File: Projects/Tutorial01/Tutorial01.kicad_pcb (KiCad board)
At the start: 2 copper layers, 42.5 x 32.5 mm, 3 parts

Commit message: commit all
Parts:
- added REF**: MountingHole_3.2mm_M3, MountingHole:MountingHole_3.2mm_M3, F.Cu at (143.5, 89.5)
- added REF**: MountingHole_3.2mm_M3, MountingHole:MountingHole_3.2mm_M3, F.Cu at (143.5, 113.5)
- added REF**: MountingHole_3.2mm_M3, MountingHole:MountingHole_3.2mm_M3, F.Cu at (109.5, 113.5)
- added REF**: MountingHole_3.2mm_M3, MountingHole:MountingHole_3.2mm_M3, F.Cu at (109.5, 89.5)
- moved R1 18.5 mm to (141.0, 106.0), turned to 90 degrees
- moved D1 9.27 mm to (134.0, 113.5)
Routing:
- net Net-(D1-K): track 26.2 -> 10.4 mm
- net Net-(Batterie1-+): track 17.3 -> 8.06 mm
- net Net-(Batterie1--): track 13.6 -> 20.3 mm

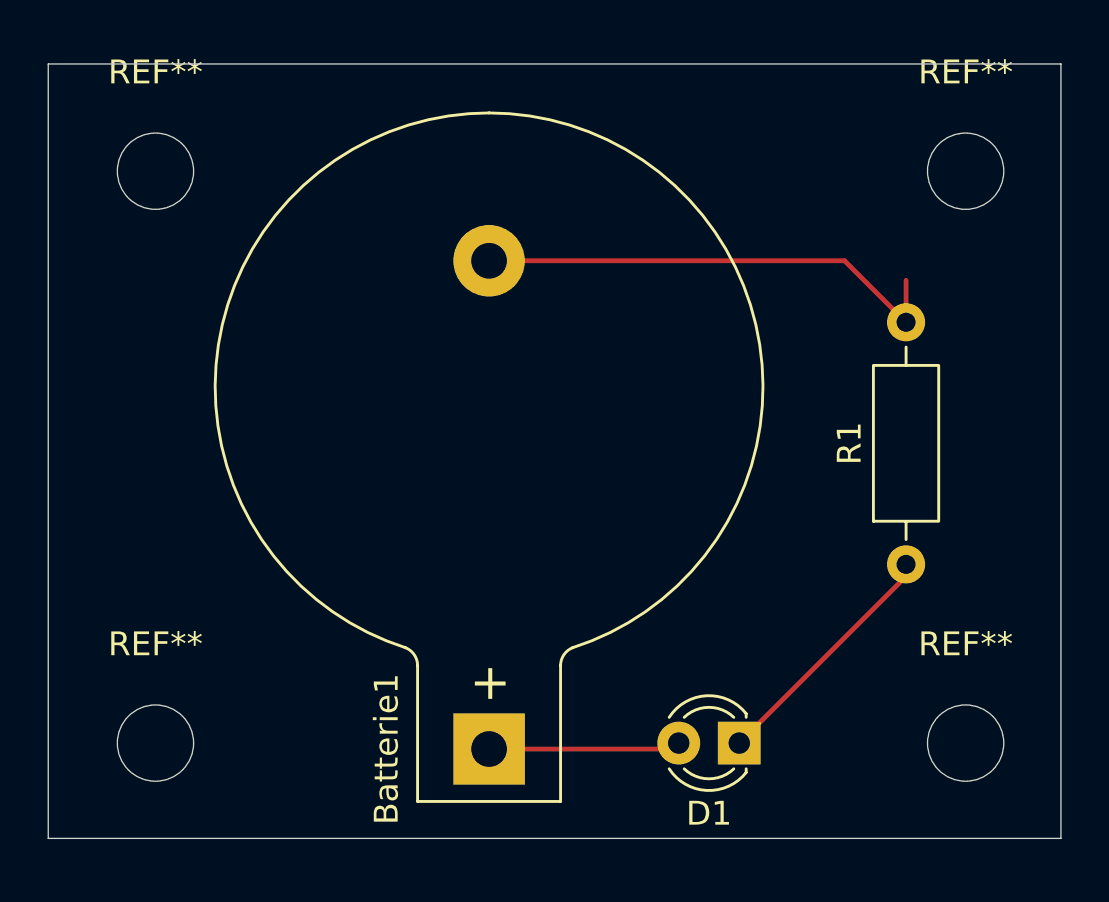
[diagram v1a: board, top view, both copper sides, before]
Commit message: 20251115 Schaltplan mit Batterie 9V, eine rote Diode 3 mm Durchmnesser und ein Widerstand 220 ohm
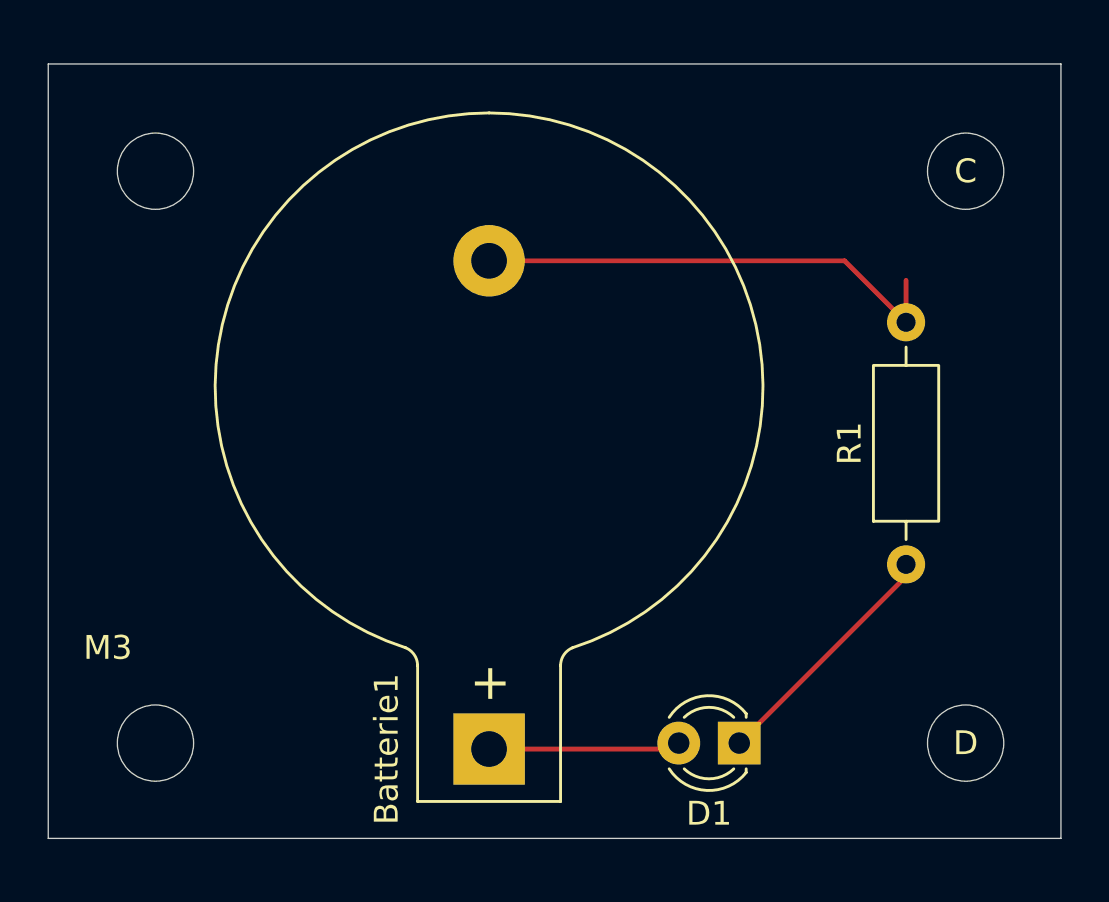
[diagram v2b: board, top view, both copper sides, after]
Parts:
- renumbered REF** to C, REF** to D, REF** to M3
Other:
- board text added: "LOGO"
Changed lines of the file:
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@@
 		(descr "Mounting Hole 3.2mm, M3, no annular, generated by kicad-footprint-generator mountinghole.py")
 		(tags "mountinghole M3")
-		(property "Reference" "REF**"
-			(at 0 -4.15 0)
+		(property "Reference" "C"
+			(at 0 0 0)
 			(layer "F.SilkS")
 			(effects
@@
 			(at 0 4.15 0)
 			(layer "F.Fab")
+			(hide yes)
 			(effects
 				(font
@@
 		(descr "Mounting Hole 3.2mm, M3, no annular, generated by kicad-footprint-generator mountinghole.py")
 		(tags "mountinghole M3")
-		(property "Reference" "REF**"
-			(at 0 -4.15 0)
+		(property "Reference" "D"
+			(at 0 0 0)
 			(layer "F.SilkS")
 			(effects
@@
 			(at 0 4.15 0)
 			(layer "F.Fab")
+			(hide yes)
 			(effects
 				(font
@@
 		(descr "Mounting Hole 3.2mm, M3, no annular, generated by kicad-footprint-generator mountinghole.py")
 		(tags "mountinghole M3")
-		(property "Reference" "REF**"
-			(at 0 -4.15 0)
+		(property "Reference" "M3"
+			(at -2 -4 0)
 			(layer "F.SilkS")
 			(effects
@@
 			(at 0 4.15 0)
 			(layer "F.Fab")
+			(hide yes)
 			(effects
 				(font
@@
 		(descr "Mounting Hole 3.2mm, M3, no annular, generated by kicad-footprint-generator mountinghole.py")
 		(tags "mountinghole M3")
-		(property "Reference" "REF**"
-			(at 0 -4.15 0)
-			(layer "F.SilkS")
+		(property "Reference" "M3"
+			(at 4.5 -3 0)
+			(layer "F.SilkS")
+			(hide yes)
 			(effects
 				(font
@@
 		)
 		(property "Value" "MountingHole_3.2mm_M3"
-			(at 0 4.15 0)
+			(at 0 -6.5 0)
 			(layer "F.Fab")
 			(effects
@@
 		(layer "Edge.Cuts")
 	)
+	(gr_text "LOGO"
+		(at 108.5 102.5 90)
+		(layer "F.Mask")
+		(effects
+			(font
+				(size 1 1)
+				(thickness 0.15)
+			)
+			(justify left bottom)
+		)
+	)
+	(gr_text "LOGO"
+		(at 146 98.5 90)
+		(layer "B.Mask")
+		(effects
+			(font
+				(size 1 1)
+				(thickness 0.15)
+			)
+			(justify left bottom mirror)
+		)
+	)
 	(segment

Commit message: 20251118 Schaltplan mit Batterie 9V, eine rote Diode 3 mm Durchmnesser und ein Widerstand 220 ohm
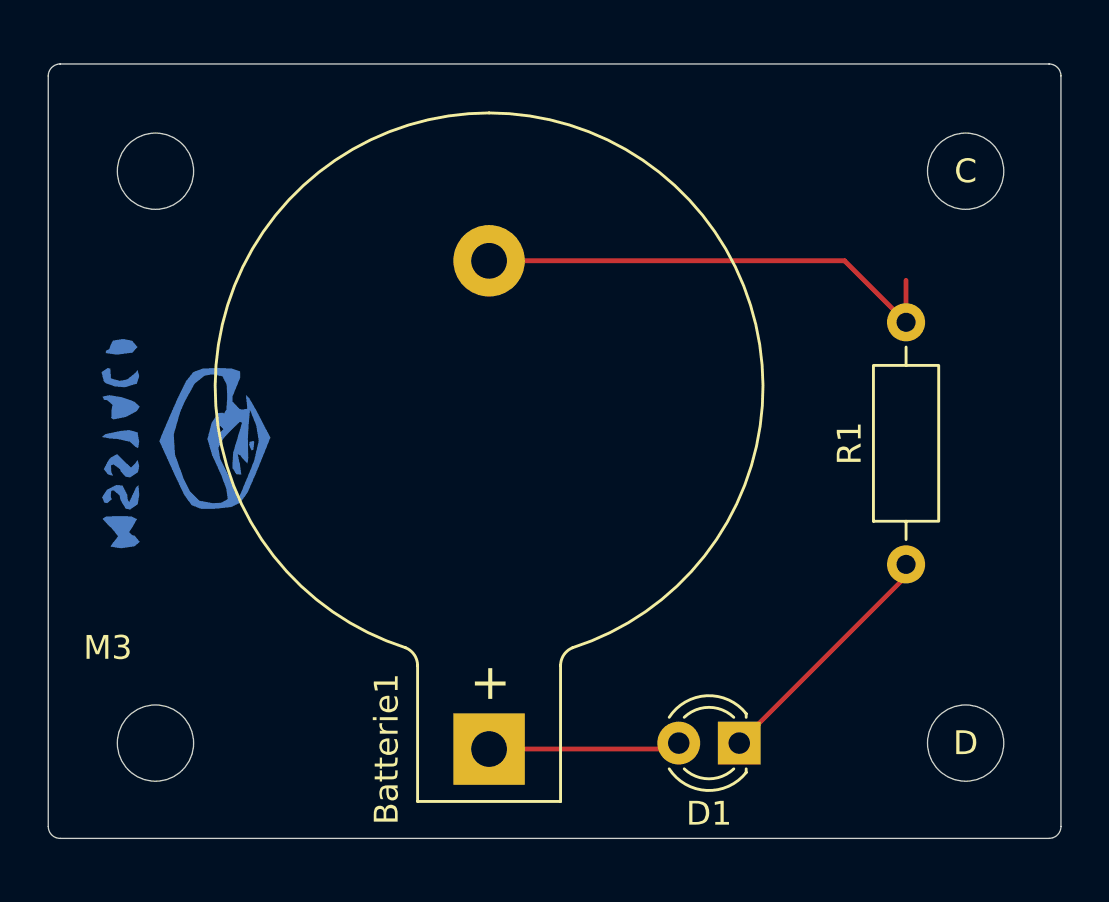
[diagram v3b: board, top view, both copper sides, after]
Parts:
- added G***: LOGO, Tutorial01:image-8-1, B.Cu at (111.0, 101.0)
- added REF**: KiCad-Logo2_5mm_SilkScreen, Symbol:KiCad-Logo2_5mm_SilkScreen, B.Cu at (124.0, 99.0)
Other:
- outline, holes or cut-outs redrawn
